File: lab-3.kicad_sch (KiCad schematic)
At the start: 43 parts, among them J1 Conn_SWD, J2 USB_C_Receptacle, J3 Conn_PORT C, J4 Conn_GND, SW1 NRST, SW2 BOOT, SW3 USER, U1 LM66100DCK, U2 LM66100DCK, U3 STM32F405RGTx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

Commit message: Add I2C
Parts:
- added J5: Conn_01x04_Pin, Connector_PinHeader_2.54mm:PinHeader_1x04_P2.54mm_Vertical, symbol Connector:Conn_01x04_Pin
- added R11, R12: 4.7k, Resistor_SMD:R_0603_1608Metric, symbol Device:R
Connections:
- net +3.3V: now also J5.1 (Pin_1), R11.1, R12.1
- net GND: now also J5.2 (Pin_2)
- net I2C1_SCL: now reaches U3.58 (PB6)
- net I2C1_SCL: now also J5.3 (Pin_3), R11.2
- net I2C1_SDA: now reaches U3.59 (PB7)
- net I2C1_SDA: now also J5.4 (Pin_4), R12.2
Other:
- note added: "GND"
- note added: "I2C"
- note added: "SCL"
- note added: "SDA"
- note added: "VCC"

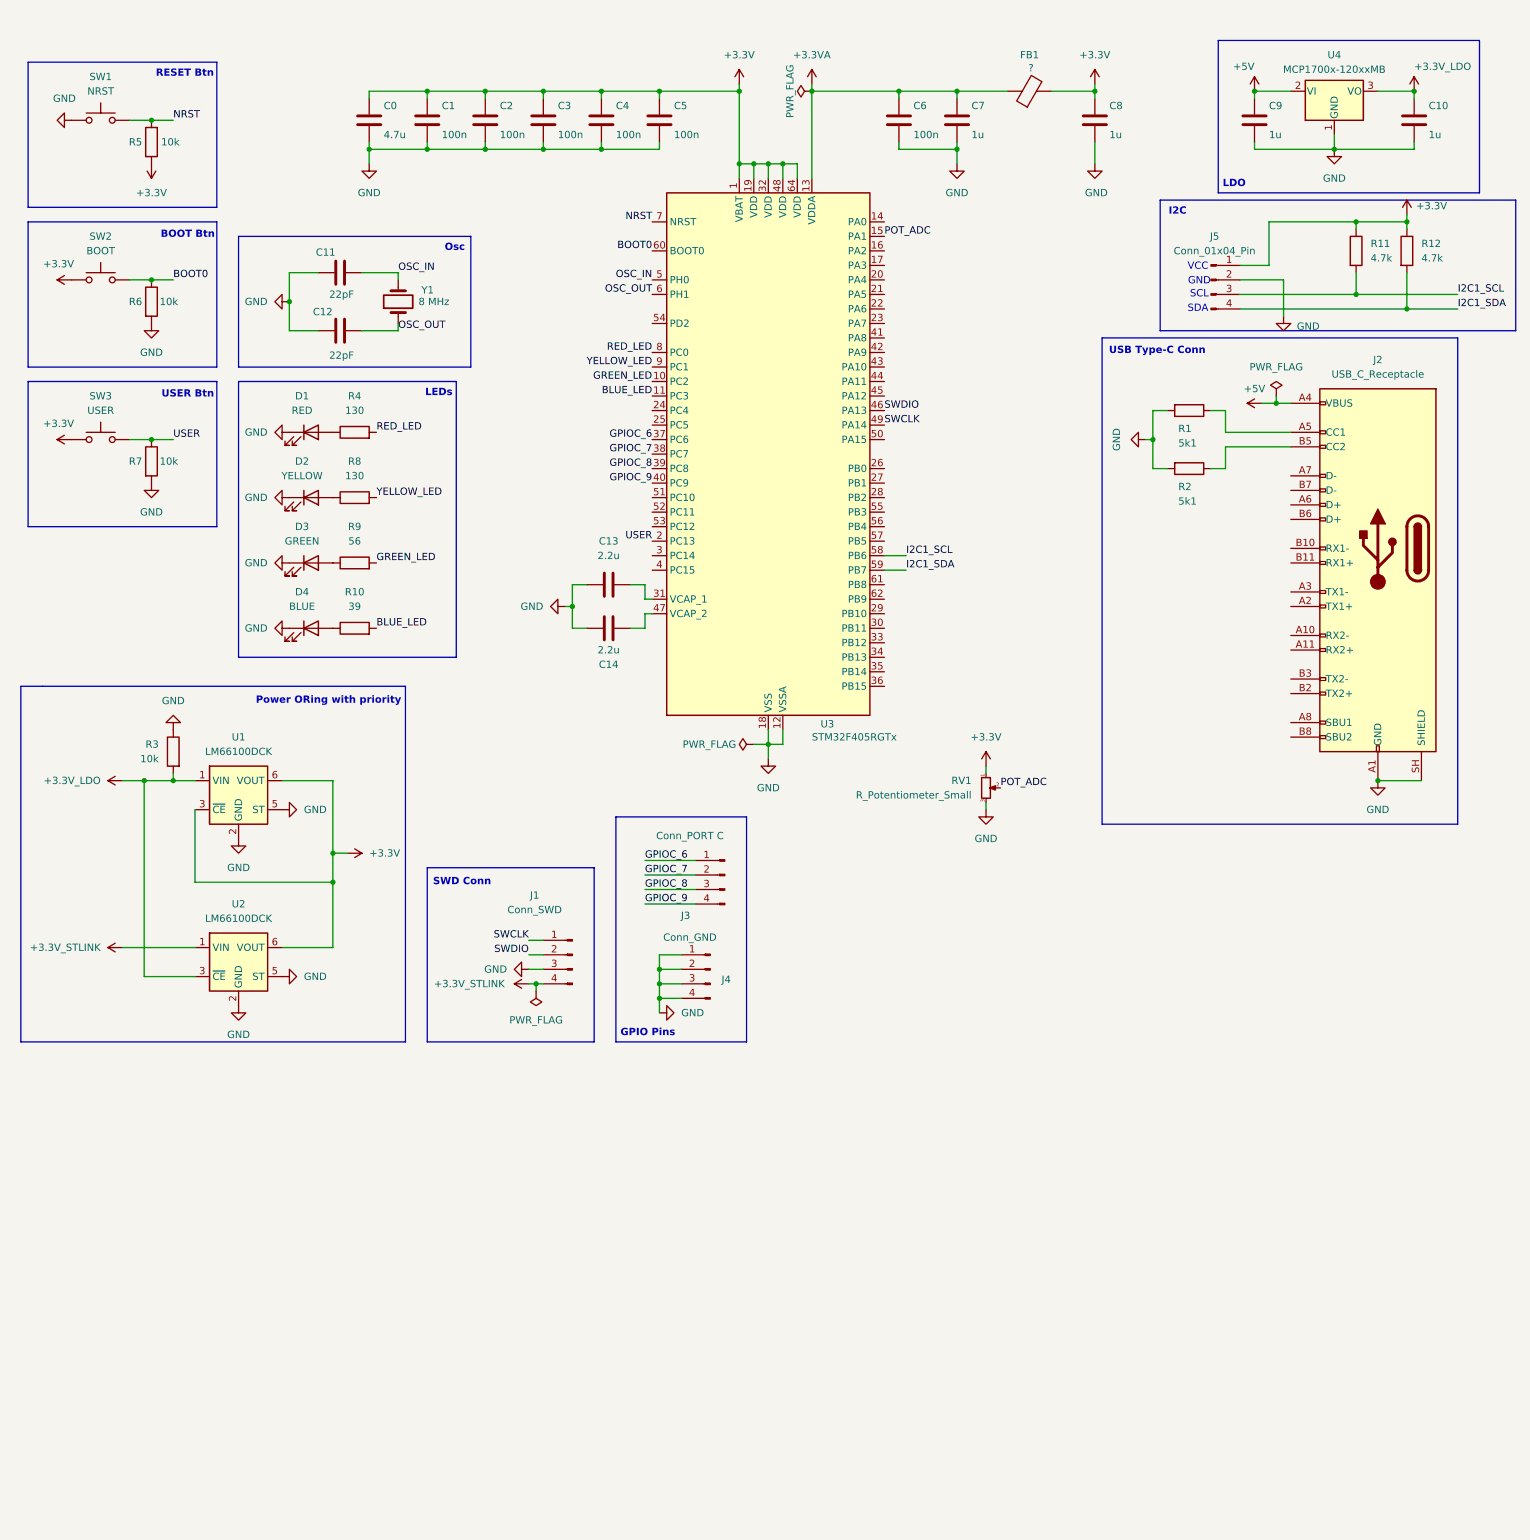
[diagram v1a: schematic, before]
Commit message: add single 1x24 pin header
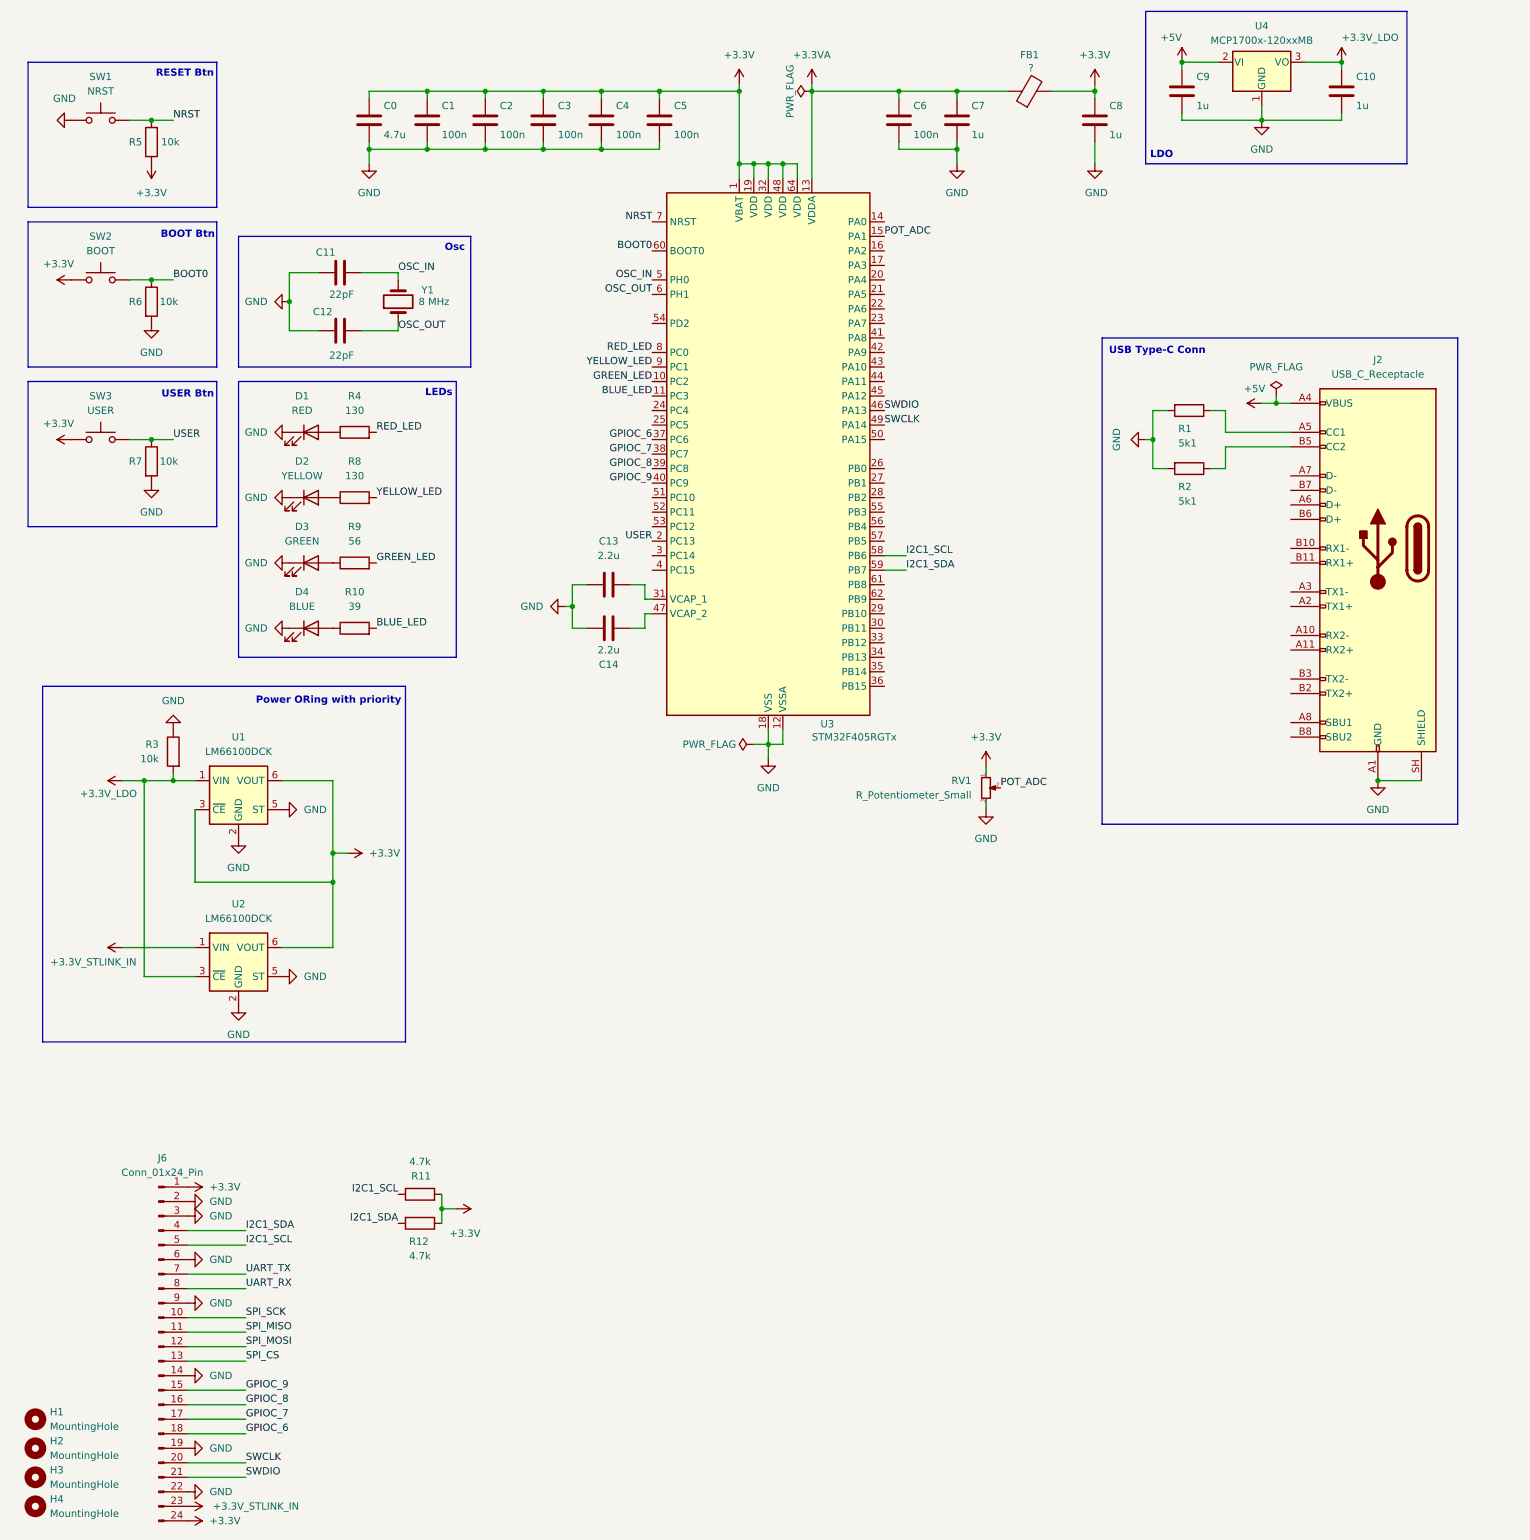
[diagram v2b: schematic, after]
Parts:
- removed J1: Conn_SWD, Connector_PinHeader_2.54mm:PinHeader_1x04_P2.54mm_Vertical, symbol Connector:Conn_01x04_Pin
- removed J3: Conn_PORT C, Connector_PinHeader_2.54mm:PinHeader_1x04_P2.54mm_Vertical, symbol Connector:Conn_01x04_Pin
- removed J4: Conn_GND, Connector_PinHeader_2.54mm:PinHeader_1x04_P2.54mm_Vertical, symbol Connector:Conn_01x04_Pin
- removed J5: Conn_01x04_Pin, Connector_PinHeader_2.54mm:PinHeader_1x04_P2.54mm_Vertical, symbol Connector:Conn_01x04_Pin
- added H1, H2, H3, H4: MountingHole, MountingHole:MountingHole_2.2mm_M2_Pad, symbol Mechanical:MountingHole
- added J6: Conn_01x24_Pin, Connector_PinHeader_2.54mm:PinHeader_1x24_P2.54mm_Vertical, symbol Connector:Conn_01x24_Pin
- R11, R12: footprint Resistor_SMD:R_0603_1608Metric -> Resistor_SMD:R_0402_1005Metric
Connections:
- net +3.3V: now also R11.2, J6.1 (Pin_1), J6.24 (Pin_24); no longer R11.1
- net GND: now also J6.14 (Pin_14), J6.19 (Pin_19), J6.2 (Pin_2), J6.22 (Pin_22), J6.3 (Pin_3), J6.6 (Pin_6), J6.9 (Pin_9)
- net GPIOC_6: now also J6.18 (Pin_18)
- net GPIOC_7: now also J6.17 (Pin_17)
- net GPIOC_8: now also J6.16 (Pin_16)
- net GPIOC_9: now also J6.15 (Pin_15)
- net I2C1_SCL: now also R11.1, J6.5 (Pin_5); no longer R11.2
- net I2C1_SDA: now also J6.4 (Pin_4)
- net SWCLK: now also J6.20 (Pin_20)
- net SWDIO: now also J6.21 (Pin_21)
- net +3.3V_STLINK renamed +3.3V_STLINK_IN
- net +3.3V_STLINK_IN: now also J6.23 (Pin_23)
- new net SPI_CS: J6.13 (Pin_13)
- new net SPI_MISO: J6.11 (Pin_11)
- new net SPI_MOSI: J6.12 (Pin_12)
- new net SPI_SCK: J6.10 (Pin_10)
- new net UART_RX: J6.8 (Pin_8)
- new net UART_TX: J6.7 (Pin_7)
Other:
- note removed: "GND"
- note removed: "GPIO Pins"
- note removed: "I2C"
- note removed: "SCL"
- note removed: "SDA"
- note removed: "SWD Conn"
- note removed: "VCC"
- moved on the sheet: C10, C9, R11, R12, U4

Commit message: add uart and spi
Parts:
- added R14: 4.7k, Resistor_SMD:R_0402_1005Metric, symbol Device:R
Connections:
- net SPI_CS is gone; now on net SPI_NSS: J6.13 (Pin_13)
- net +3.3V: now also R14.2
- net SPI_MISO: now also U3.35 (PB14)
- net SPI_MOSI: now also J6.10 (Pin_10), U3.36 (PB15); no longer J6.12 (Pin_12)
- net SPI_SCK: now also J6.12 (Pin_12), U3.34 (PB13); no longer J6.10 (Pin_10)
- net UART_RX: now also J6.7 (Pin_7), U3.52 (PC11); no longer J6.8 (Pin_8)
- net UART_TX: now also J6.8 (Pin_8), U3.51 (PC10); no longer J6.7 (Pin_7)
- net SPI_NSS: now reaches U3.33 (PB12)
- net SPI_NSS: now also R14.1

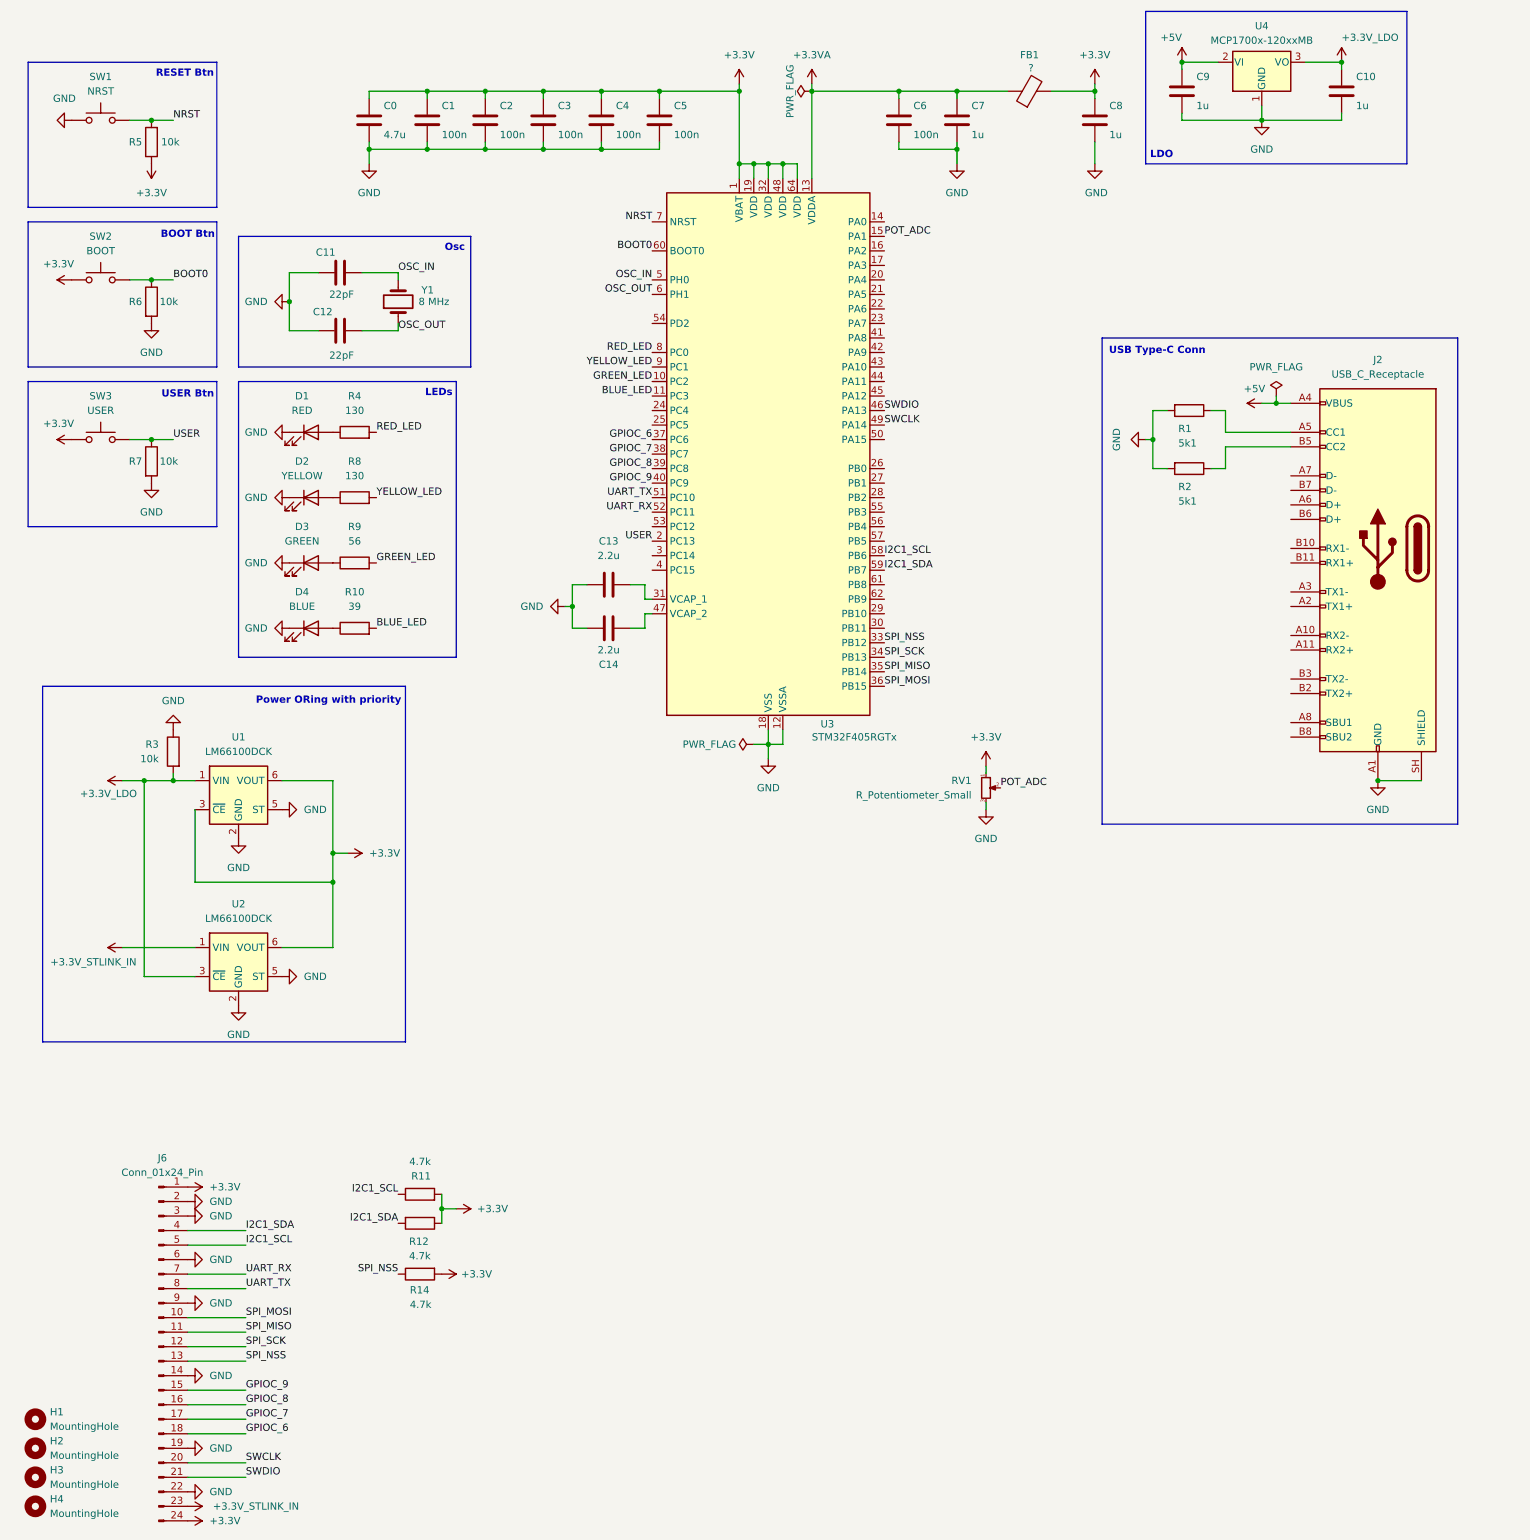
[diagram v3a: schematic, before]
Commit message: fix i2c and spi trace length
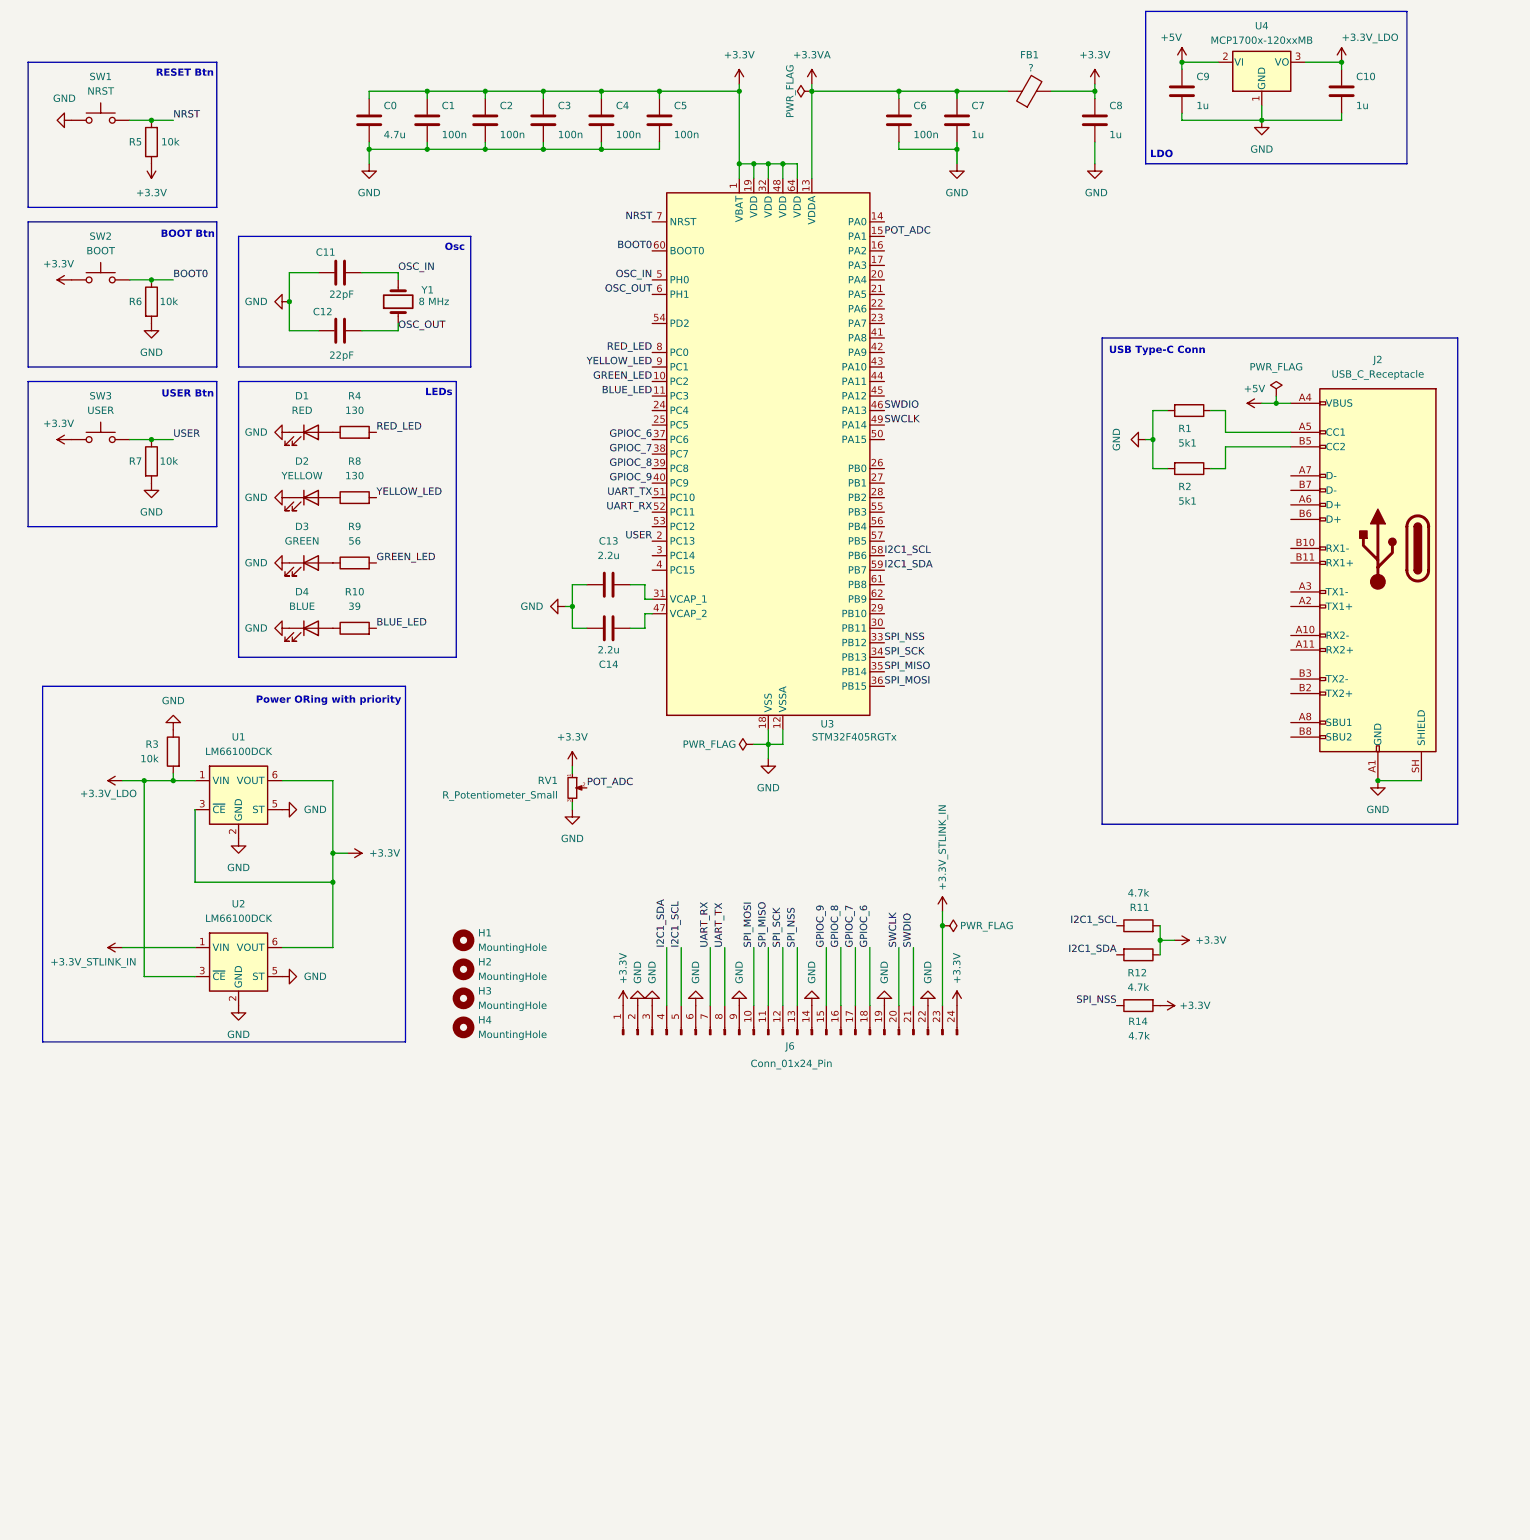
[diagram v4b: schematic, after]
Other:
- moved on the sheet: RV1
